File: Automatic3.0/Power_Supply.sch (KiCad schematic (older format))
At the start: 19 parts, among them J1 CONN_01X02, U1 Buck, U2 LM7809

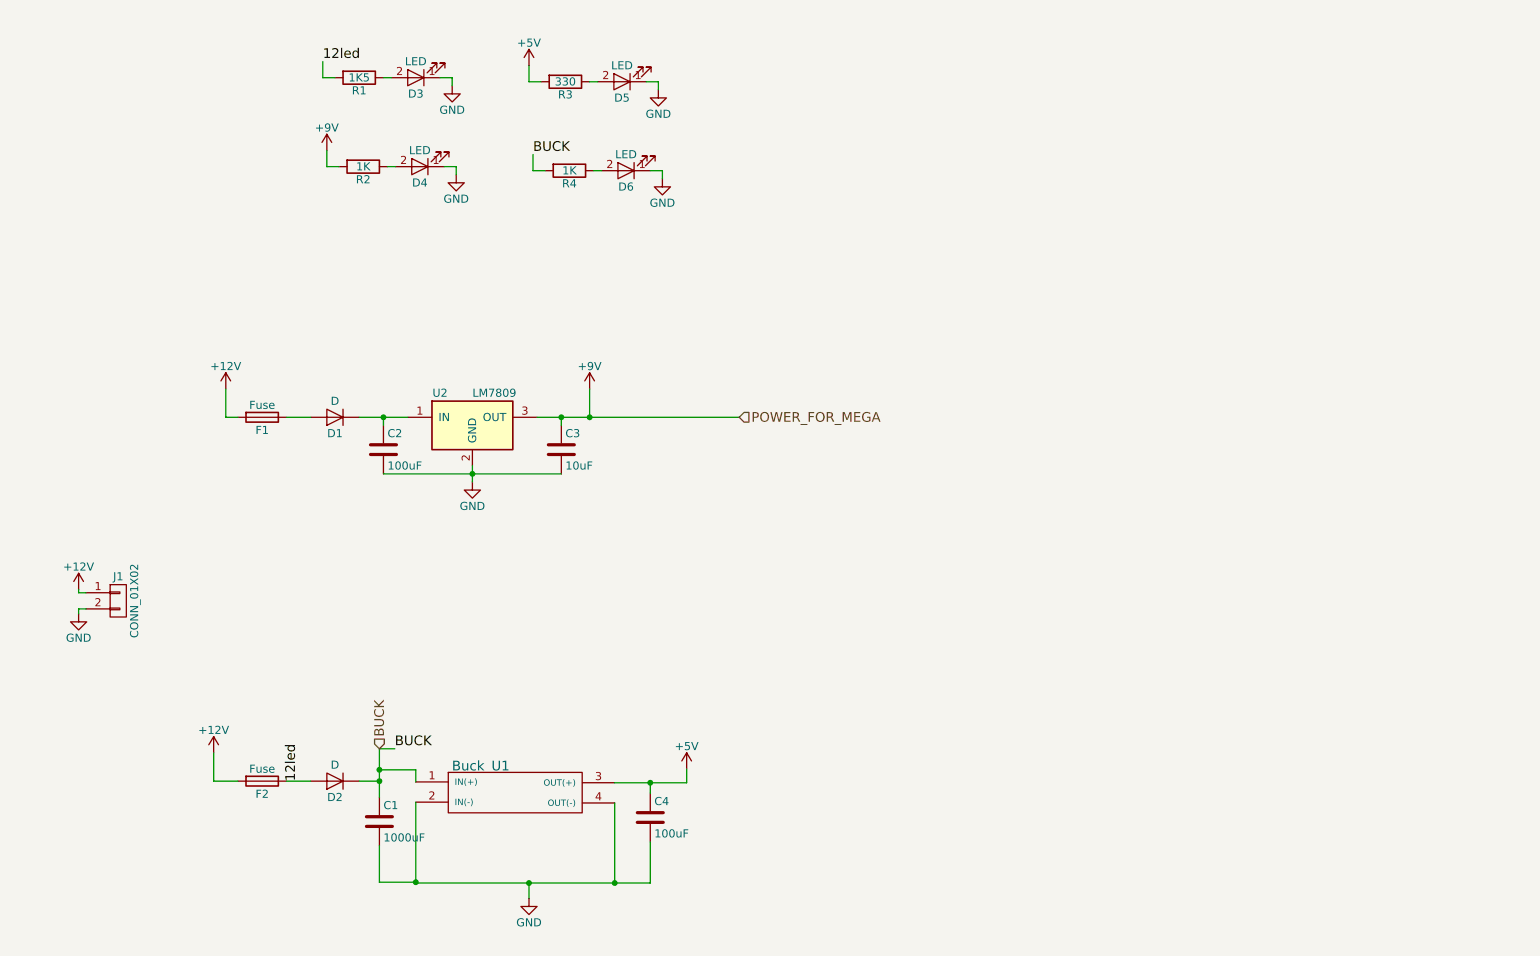
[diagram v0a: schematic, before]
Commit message: Created new schemetic for automatic
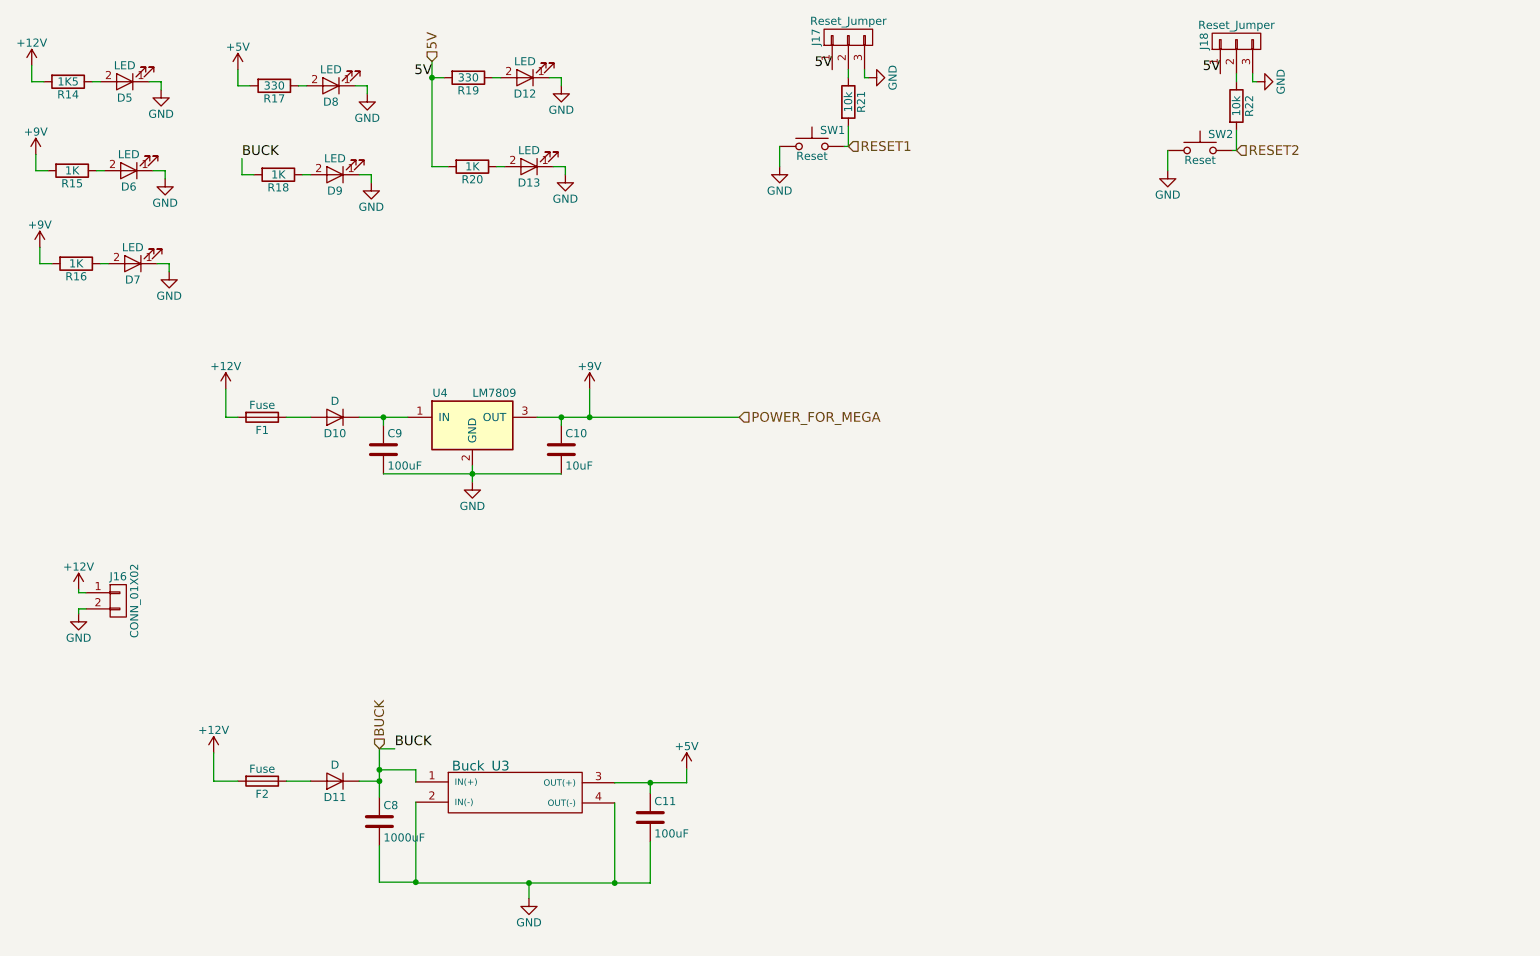
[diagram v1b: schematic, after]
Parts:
- added D12, D13, D7: LED, modFiles:LED_D3.0mm, symbol LED
- added J17, J18: Reset_Jumper, Pin_Headers:Pin_Header_Straight_1x03_Pitch2.54mm, symbol CONN_01X03
- added R16, R20: 1K, modFiles:Resistor_small, symbol R
- added R19: 330, Resistors_THT:R_Axial_DIN0207_L6.3mm_D2.5mm_P10.16mm_Horizontal, symbol R
- added R21, R22: 10k, modFiles:Resistor_small, symbol R
- added SW1, SW2: Reset, modFiles:Push_Button, symbol SW_Push
- renumbered C3 to C10, C4 to C11, C1 to C8, C2 to C9, D1 to D10, D2 to D11, D3 to D5, D4 to D6, D5 to D8, D6 to D9, J1 to J16, R1 to R14, R2 to R15, R3 to R17, R4 to R18, U1 to U3, U2 to U4
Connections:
- net +12V: now also R14.2
- net +9V: now also R16.2
- net GND: now also D12.1 (K), D13.1 (K), D7.1 (K), J17.3 (P3), J18.3 (P3), SW1.1, SW2.1
- net 12led: no longer names the net of D11.2 (A), F2.1
- net 12led: no longer R14.2
- new net: D12.2 (A), R19.1
- new net: D13.2 (A), R20.1
- new net: J17.2 (P2), R21.1
- new net: J18.2 (P2), R22.1
- new net: D7.2 (A), R16.1
- new net 5V: J17.1 (P1), J18.1 (P1), R19.2, R20.2
- new net RESET1: R21.2, SW1.2
- new net RESET2: R22.2, SW2.2
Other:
- moved on the sheet: D5, D6, D8, D9, R14, R15, R17, R18

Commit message: Modified the automatic circuit
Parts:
- D12, D13, D8: value LED -> LED_5V
- D5: value LED -> LED_12V
- D6: value LED -> LED_9V
- D9: value LED -> LED_BUCK
- R17, R19: footprint Resistors_THT:R_Axial_DIN0207_L6.3mm_D2.5mm_P10.16mm_Horizontal -> modFiles:Resistor_small
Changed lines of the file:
@@
 LIBS:zetex
 LIBS:Zilog
-LIBS:Automatic3-cache
+LIBS:Power_Supply-cache
 EELAYER 25 0
 EELAYER END
 $Descr A4 11693 8268
 encoding utf-8
-Sheet 1 2
+Sheet 1 1
 Title ""
 Date ""
@@
 $EndDescr
 $Comp
-L +12V #PWR030
+L +12V #PWR035
 U 1 1 5ADD8405
 P 1400 1225
-F 0 "#PWR030" H 1400 1075 50  0001 C CNN
+F 0 "#PWR035" H 1400 1075 50  0001 C CNN
 F 1 "+12V" H 1400 1365 50  0000 C CNN
 F 2 "" H 1400 1225 50  0001 C CNN
@@
 F 0 "R17" V 2980 1350 50  0000 C CNN
 F 1 "330" V 2900 1350 50  0000 C CNN
-F 2 "Resistors_THT:R_Axial_DIN0207_L6.3mm_D2.5mm_P10.16mm_Horizontal" V 2830 1350 50  0001 C CNN
+F 2 "modFiles:Resistor_small" V 2830 1350 50  0001 C CNN
 F 3 "" H 2900 1350 50  0001 C CNN
 	1    2900 1350
@@
 P 3250 1350
 F 0 "D8" H 3250 1450 50  0000 C CNN
-F 1 "LED" H 3250 1250 50  0000 C CNN
+F 1 "LED_5V" H 3250 1250 50  0000 C CNN
 F 2 "modFiles:LED_D3.0mm" H 3250 1350 50  0001 C CNN
 F 3 "" H 3250 1350 50  0001 C CNN
@@
 $EndComp
 $Comp
-L GND #PWR031
+L GND #PWR036
 U 1 1 5ADD84AA
 P 3475 1400
-F 0 "#PWR031" H 3475 1150 50  0001 C CNN
+F 0 "#PWR036" H 3475 1150 50  0001 C CNN
 F 1 "GND" H 3475 1250 50  0000 C CNN
 F 2 "" H 3475 1400 50  0001 C CNN
@@
 P 3275 1900
 F 0 "D9" H 3275 2000 50  0000 C CNN
-F 1 "LED" H 3275 1800 50  0000 C CNN
+F 1 "LED_BUCK" H 3275 1800 50  0000 C CNN
 F 2 "modFiles:LED_D3.0mm" H 3275 1900 50  0001 C CNN
 F 3 "" H 3275 1900 50  0001 C CNN
@@
 $EndComp
 $Comp
-L GND #PWR032
+L GND #PWR037
 U 1 1 5ADD8645
 P 3500 1950
-F 0 "#PWR032" H 3500 1700 50  0001 C CNN
+F 0 "#PWR037" H 3500 1700 50  0001 C CNN
 F 1 "GND" H 3500 1800 50  0000 C CNN
 F 2 "" H 3500 1950 50  0001 C CNN
@@
 P 1975 1325
 F 0 "D5" H 1975 1425 50  0000 C CNN
-F 1 "LED" H 1975 1225 50  0000 C CNN
+F 1 "LED_12V" H 1975 1225 50  0000 C CNN
 F 2 "modFiles:LED_D3.0mm" H 1975 1325 50  0001 C CNN
 F 3 "" H 1975 1325 50  0001 C CNN
@@
 $EndComp
 $Comp
-L GND #PWR033
+L GND #PWR038
 U 1 1 5ADD88DA
 P 2200 1375
-F 0 "#PWR033" H 2200 1125 50  0001 C CNN
+F 0 "#PWR038" H 2200 1125 50  0001 C CNN
 F 1 "GND" H 2200 1225 50  0000 C CNN
 F 2 "" H 2200 1375 50  0001 C CNN
@@
 P 2000 1875
 F 0 "D6" H 2000 1975 50  0000 C CNN
-F 1 "LED" H 2000 1775 50  0000 C CNN
+F 1 "LED_9V" H 2000 1775 50  0000 C CNN
 F 2 "modFiles:LED_D3.0mm" H 2000 1875 50  0001 C CNN
 F 3 "" H 2000 1875 50  0001 C CNN
@@
 $EndComp
 $Comp
-L GND #PWR034
+L GND #PWR039
 U 1 1 5ADD88F7
 P 2225 1925
-F 0 "#PWR034" H 2225 1675 50  0001 C CNN
+F 0 "#PWR039" H 2225 1675 50  0001 C CNN
 F 1 "GND" H 2225 1775 50  0000 C CNN
 F 2 "" H 2225 1925 50  0001 C CNN
@@
 $EndComp
 $Comp
-L +9V #PWR035
+L +9V #PWR040
 U 1 1 5ADD8969
 P 1425 1775
-F 0 "#PWR035" H 1425 1625 50  0001 C CNN
+F 0 "#PWR040" H 1425 1625 50  0001 C CNN
 F 1 "+9V" H 1425 1915 50  0000 C CNN
 F 2 "" H 1425 1775 50  0001 C CNN
@@
 $EndComp
 $Comp
-L +5V #PWR036
+L +5V #PWR041
 U 1 1 5ADD89A5
 P 2675 1250
-F 0 "#PWR036" H 2675 1100 50  0001 C CNN
+F 0 "#PWR041" H 2675 1100 50  0001 C CNN
 F 1 "+5V" H 2675 1390 50  0000 C CNN
 F 2 "" H 2675 1250 50  0001 C CNN
@@
 $EndComp
 $Comp
-L +12V #PWR037
+L +12V #PWR042
 U 1 1 5ADD8D0E
 P 2600 3225
-F 0 "#PWR037" H 2600 3075 50  0001 C CNN
+F 0 "#PWR042" H 2600 3075 50  0001 C CNN
 F 1 "+12V" H 2600 3365 50  0000 C CNN
 F 2 "" H 2600 3225 50  0001 C CNN
@@
 $EndComp
 $Comp
-L +9V #PWR038
+L +9V #PWR043
 U 1 1 5ADD8DBB
 P 4850 3225
-F 0 "#PWR038" H 4850 3075 50  0001 C CNN
+F 0 "#PWR043" H 4850 3075 50  0001 C CNN
 F 1 "+9V" H 4850 3365 50  0000 C CNN
 F 2 "" H 4850 3225 50  0001 C CNN
@@
 POWER_FOR_MEGA
 $Comp
-L GND #PWR039
+L GND #PWR044
 U 1 1 5ADD935A
 P 4125 3800
-F 0 "#PWR039" H 4125 3550 50  0001 C CNN
+F 0 "#PWR044" H 4125 3550 50  0001 C CNN
 F 1 "GND" H 4125 3650 50  0000 C CNN
 F 2 "" H 4125 3800 50  0001 C CNN
@@
 $EndComp
 $Comp
-L +12V #PWR040
+L +12V #PWR045
 U 1 1 5ADDA23F
 P 2525 5475
-F 0 "#PWR040" H 2525 5325 50  0001 C CNN
+F 0 "#PWR045" H 2525 5325 50  0001 C CNN
 F 1 "+12V" H 2525 5615 50  0000 C CNN
 F 2 "" H 2525 5475 50  0001 C CNN
@@
 $EndComp
 $Comp
-L GND #PWR041
+L GND #PWR046
 U 1 1 5ADDA376
 P 4475 6375
-F 0 "#PWR041" H 4475 6125 50  0001 C CNN
+F 0 "#PWR046" H 4475 6125 50  0001 C CNN
 F 1 "GND" H 4475 6225 50  0000 C CNN
 F 2 "" H 4475 6375 50  0001 C CNN
@@
 $EndComp
 $Comp
-L +5V #PWR042
+L +5V #PWR047
 U 1 1 5ADDA3B0
 P 5450 5575
-F 0 "#PWR042" H 5450 5425 50  0001 C CNN
+F 0 "#PWR047" H 5450 5425 50  0001 C CNN
 F 1 "+5V" H 5450 5715 50  0000 C CNN
 F 2 "" H 5450 5575 50  0001 C CNN
@@
 $EndComp
 $Comp
-L +12V #PWR043
+L +12V #PWR048
 U 1 1 5ADDD1E7
 P 1690 4465
-F 0 "#PWR043" H 1690 4315 50  0001 C CNN
+F 0 "#PWR048" H 1690 4315 50  0001 C CNN
 F 1 "+12V" H 1690 4605 50  0000 C CNN
 F 2 "" H 1690 4465 50  0001 C CNN
@@
 $EndComp
 $Comp
-L GND #PWR044
+L GND #PWR049
 U 1 1 5ADDD3BB
 P 1690 4615
-F 0 "#PWR044" H 1690 4365 50  0001 C CNN
+F 0 "#PWR049" H 1690 4365 50  0001 C CNN
 F 1 "GND" H 1690 4465 50  0000 C CNN
 F 2 "" H 1690 4615 50  0001 C CNN
@@
 F 0 "R19" V 4180 1300 50  0000 C CNN
 F 1 "330" V 4100 1300 50  0000 C CNN
-F 2 "Resistors_THT:R_Axial_DIN0207_L6.3mm_D2.5mm_P10.16mm_Horizontal" V 4030 1300 50  0001 C CNN
+F 2 "modFiles:Resistor_small" V 4030 1300 50  0001 C CNN
 F 3 "" H 4100 1300 50  0001 C CNN
 	1    4100 1300
@@
 P 4450 1300
 F 0 "D12" H 4450 1400 50  0000 C CNN
-F 1 "LED" H 4450 1200 50  0000 C CNN
+F 1 "LED_5V" H 4450 1200 50  0000 C CNN
 F 2 "modFiles:LED_D3.0mm" H 4450 1300 50  0001 C CNN
 F 3 "" H 4450 1300 50  0001 C CNN
@@
 $EndComp
 $Comp
-L GND #PWR045
+L GND #PWR050
 U 1 1 5B1412F8
 P 4675 1350
-F 0 "#PWR045" H 4675 1100 50  0001 C CNN
+F 0 "#PWR050" H 4675 1100 50  0001 C CNN
 F 1 "GND" H 4675 1200 50  0000 C CNN
 F 2 "" H 4675 1350 50  0001 C CNN
@@
 P 4475 1850
 F 0 "D13" H 4475 1950 50  0000 C CNN
-F 1 "LED" H 4475 1750 50  0000 C CNN
+F 1 "LED_5V" H 4475 1750 50  0000 C CNN
 F 2 "modFiles:LED_D3.0mm" H 4475 1850 50  0001 C CNN
 F 3 "" H 4475 1850 50  0001 C CNN
@@
 $EndComp
 $Comp
-L GND #PWR046
+L GND #PWR051
 U 1 1 5B14130A
 P 4700 1900
-F 0 "#PWR046" H 4700 1650 50  0001 C CNN
+F 0 "#PWR051" H 4700 1650 50  0001 C CNN
 F 1 "GND" H 4700 1750 50  0000 C CNN
 F 2 "" H 4700 1900 50  0001 C CNN
@@
 $EndComp
 $Comp
-L GND #PWR047
+L GND #PWR052
 U 1 1 5B1417E4
 P 6025 1850
-F 0 "#PWR047" H 6025 1600 50  0001 C CNN
+F 0 "#PWR052" H 6025 1600 50  0001 C CNN
 F 1 "GND" H 6025 1700 50  0000 C CNN
 F 2 "" H 6025 1850 50  0001 C CNN
@@
 5V
 $Comp
-L GND #PWR048
+L GND #PWR053
 U 1 1 5B14194B
 P 6575 1300
-F 0 "#PWR048" H 6575 1050 50  0001 C CNN
+F 0 "#PWR053" H 6575 1050 50  0001 C CNN
 F 1 "GND" H 6575 1150 50  0000 C CNN
 F 2 "" H 6575 1300 50  0001 C CNN
@@
 $EndComp
 $Comp
-L GND #PWR049
+L GND #PWR054
 U 1 1 5B142045
 P 8425 1875
-F 0 "#PWR049" H 8425 1625 50  0001 C CNN
+F 0 "#PWR054" H 8425 1625 50  0001 C CNN
 F 1 "GND" H 8425 1725 50  0000 C CNN
 F 2 "" H 8425 1875 50  0001 C CNN
@@
 5V
 $Comp
-L GND #PWR050
+L GND #PWR055
 U 1 1 5B14204C
 P 8975 1325
-F 0 "#PWR050" H 8975 1075 50  0001 C CNN
+F 0 "#PWR055" H 8975 1075 50  0001 C CNN
 F 1 "GND" H 8975 1175 50  0000 C CNN
 F 2 "" H 8975 1325 50  0001 C CNN
@@
 $EndComp
 $Comp
-L GND #PWR051
+L GND #PWR056
 U 1 1 5B14315F
 P 2250 2500
-F 0 "#PWR051" H 2250 2250 50  0001 C CNN
+F 0 "#PWR056" H 2250 2250 50  0001 C CNN
 F 1 "GND" H 2250 2350 50  0000 C CNN
 F 2 "" H 2250 2500 50  0001 C CNN
@@
 $EndComp
 $Comp
-L +9V #PWR052
+L +9V #PWR057
 U 1 1 5B143165
 P 1450 2350
-F 0 "#PWR052" H 1450 2200 50  0001 C CNN
+F 0 "#PWR057" H 1450 2200 50  0001 C CNN
 F 1 "+9V" H 1450 2490 50  0000 C CNN
 F 2 "" H 1450 2350 50  0001 C CNN

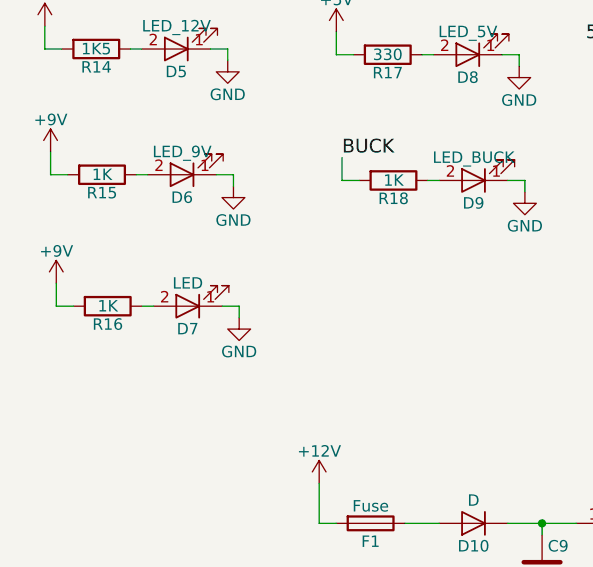
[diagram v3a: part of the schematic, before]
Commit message: added the jst connector
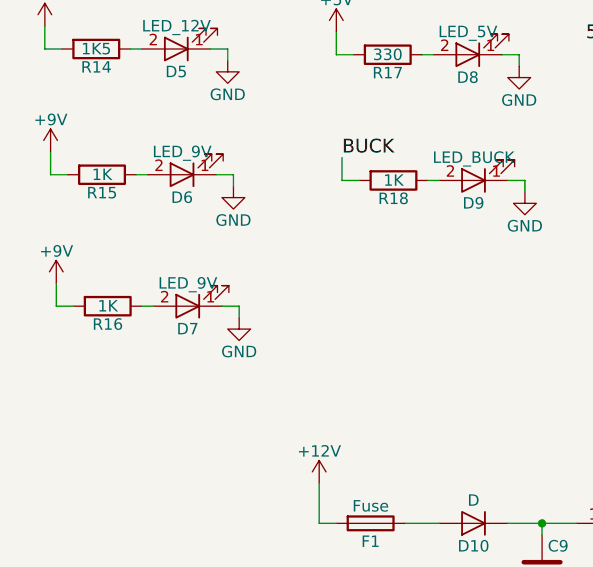
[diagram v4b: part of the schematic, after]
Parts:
- D7: value LED -> LED_9V
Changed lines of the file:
@@
 LIBS:contrib
 LIBS:valves
-LIBS:Prashant_library
 LIBS:74xgxx
 LIBS:ac-dc
@@
 LIBS:ftdi
 LIBS:gennum
-LIBS:graphic
 LIBS:hc11
 LIBS:ir
 LIBS:Lattice
 LIBS:leds
-LIBS:logo
 LIBS:maxim
 LIBS:mechanical
@@
 LIBS:zetex
 LIBS:Zilog
+LIBS:Prashant_library
 LIBS:Automatic3-cache
 EELAYER 25 0
@@
 $Descr A4 11693 8268
 encoding utf-8
-Sheet 1 2
+Sheet 2 2
 Title ""
 Date ""
@@
 $EndDescr
 $Comp
-L +12V #PWR043
+L +12V #PWR044
 U 1 1 5ADD8405
 P 1400 1225
-F 0 "#PWR043" H 1400 1075 50  0001 C CNN
+F 0 "#PWR044" H 1400 1075 50  0001 C CNN
 F 1 "+12V" H 1400 1365 50  0000 C CNN
 F 2 "" H 1400 1225 50  0001 C CNN
@@
 $EndComp
 $Comp
-L GND #PWR044
+L GND #PWR045
 U 1 1 5ADD84AA
 P 3475 1400
-F 0 "#PWR044" H 3475 1150 50  0001 C CNN
+F 0 "#PWR045" H 3475 1150 50  0001 C CNN
 F 1 "GND" H 3475 1250 50  0000 C CNN
 F 2 "" H 3475 1400 50  0001 C CNN
@@
 $EndComp
 $Comp
-L GND #PWR045
+L GND #PWR046
 U 1 1 5ADD8645
 P 3500 1950
-F 0 "#PWR045" H 3500 1700 50  0001 C CNN
+F 0 "#PWR046" H 3500 1700 50  0001 C CNN
 F 1 "GND" H 3500 1800 50  0000 C CNN
 F 2 "" H 3500 1950 50  0001 C CNN
@@
 $EndComp
 $Comp
-L GND #PWR046
+L GND #PWR047
 U 1 1 5ADD88DA
 P 2200 1375
-F 0 "#PWR046" H 2200 1125 50  0001 C CNN
+F 0 "#PWR047" H 2200 1125 50  0001 C CNN
 F 1 "GND" H 2200 1225 50  0000 C CNN
 F 2 "" H 2200 1375 50  0001 C CNN
@@
 $EndComp
 $Comp
-L GND #PWR047
+L GND #PWR048
 U 1 1 5ADD88F7
 P 2225 1925
-F 0 "#PWR047" H 2225 1675 50  0001 C CNN
+F 0 "#PWR048" H 2225 1675 50  0001 C CNN
 F 1 "GND" H 2225 1775 50  0000 C CNN
 F 2 "" H 2225 1925 50  0001 C CNN
@@
 $EndComp
 $Comp
-L +9V #PWR048
+L +9V #PWR049
 U 1 1 5ADD8969
 P 1425 1775
-F 0 "#PWR048" H 1425 1625 50  0001 C CNN
+F 0 "#PWR049" H 1425 1625 50  0001 C CNN
 F 1 "+9V" H 1425 1915 50  0000 C CNN
 F 2 "" H 1425 1775 50  0001 C CNN
@@
 $EndComp
 $Comp
-L +5V #PWR049
+L +5V #PWR050
 U 1 1 5ADD89A5
 P 2675 1250
-F 0 "#PWR049" H 2675 1100 50  0001 C CNN
+F 0 "#PWR050" H 2675 1100 50  0001 C CNN
 F 1 "+5V" H 2675 1390 50  0000 C CNN
 F 2 "" H 2675 1250 50  0001 C CNN
@@
 $EndComp
 $Comp
-L +12V #PWR050
+L +12V #PWR051
 U 1 1 5ADD8D0E
 P 2600 3225
-F 0 "#PWR050" H 2600 3075 50  0001 C CNN
+F 0 "#PWR051" H 2600 3075 50  0001 C CNN
 F 1 "+12V" H 2600 3365 50  0000 C CNN
 F 2 "" H 2600 3225 50  0001 C CNN
@@
 $EndComp
 $Comp
-L +9V #PWR051
+L +9V #PWR052
 U 1 1 5ADD8DBB
 P 4850 3225
-F 0 "#PWR051" H 4850 3075 50  0001 C CNN
+F 0 "#PWR052" H 4850 3075 50  0001 C CNN
 F 1 "+9V" H 4850 3365 50  0000 C CNN
 F 2 "" H 4850 3225 50  0001 C CNN
@@
 POWER_FOR_MEGA
 $Comp
-L GND #PWR052
+L GND #PWR053
 U 1 1 5ADD935A
 P 4125 3800
-F 0 "#PWR052" H 4125 3550 50  0001 C CNN
+F 0 "#PWR053" H 4125 3550 50  0001 C CNN
 F 1 "GND" H 4125 3650 50  0000 C CNN
 F 2 "" H 4125 3800 50  0001 C CNN
@@
 $EndComp
 $Comp
-L +12V #PWR053
+L +12V #PWR054
 U 1 1 5ADDA23F
 P 2525 5475
-F 0 "#PWR053" H 2525 5325 50  0001 C CNN
+F 0 "#PWR054" H 2525 5325 50  0001 C CNN
 F 1 "+12V" H 2525 5615 50  0000 C CNN
 F 2 "" H 2525 5475 50  0001 C CNN
@@
 $EndComp
 $Comp
-L GND #PWR054
+L GND #PWR055
 U 1 1 5ADDA376
 P 4475 6375
-F 0 "#PWR054" H 4475 6125 50  0001 C CNN
+F 0 "#PWR055" H 4475 6125 50  0001 C CNN
 F 1 "GND" H 4475 6225 50  0000 C CNN
 F 2 "" H 4475 6375 50  0001 C CNN
@@
 $EndComp
 $Comp
-L +5V #PWR055
+L +5V #PWR056
 U 1 1 5ADDA3B0
 P 5450 5575
-F 0 "#PWR055" H 5450 5425 50  0001 C CNN
+F 0 "#PWR056" H 5450 5425 50  0001 C CNN
 F 1 "+5V" H 5450 5715 50  0000 C CNN
 F 2 "" H 5450 5575 50  0001 C CNN
@@
 $EndComp
 $Comp
-L +12V #PWR056
+L +12V #PWR057
 U 1 1 5ADDD1E7
 P 1690 4465
-F 0 "#PWR056" H 1690 4315 50  0001 C CNN
+F 0 "#PWR057" H 1690 4315 50  0001 C CNN
 F 1 "+12V" H 1690 4605 50  0000 C CNN
 F 2 "" H 1690 4465 50  0001 C CNN
@@
 $EndComp
 $Comp
-L GND #PWR057
+L GND #PWR058
 U 1 1 5ADDD3BB
 P 1690 4615
-F 0 "#PWR057" H 1690 4365 50  0001 C CNN
+F 0 "#PWR058" H 1690 4365 50  0001 C CNN
 F 1 "GND" H 1690 4465 50  0000 C CNN
 F 2 "" H 1690 4615 50  0001 C CNN
@@
 $EndComp
 $Comp
-L GND #PWR058
+L GND #PWR059
 U 1 1 5B1412F8
 P 4675 1350
-F 0 "#PWR058" H 4675 1100 50  0001 C CNN
+F 0 "#PWR059" H 4675 1100 50  0001 C CNN
 F 1 "GND" H 4675 1200 50  0000 C CNN
 F 2 "" H 4675 1350 50  0001 C CNN
@@
 $EndComp
 $Comp
-L GND #PWR059
+L GND #PWR060
 U 1 1 5B14130A
 P 4700 1900
-F 0 "#PWR059" H 4700 1650 50  0001 C CNN
+F 0 "#PWR060" H 4700 1650 50  0001 C CNN
 F 1 "GND" H 4700 1750 50  0000 C CNN
 F 2 "" H 4700 1900 50  0001 C CNN
@@
 $EndComp
 $Comp
-L GND #PWR060
+L GND #PWR061
 U 1 1 5B1417E4
 P 6025 1850
-F 0 "#PWR060" H 6025 1600 50  0001 C CNN
+F 0 "#PWR061" H 6025 1600 50  0001 C CNN
 F 1 "GND" H 6025 1700 50  0000 C CNN
 F 2 "" H 6025 1850 50  0001 C CNN
@@
 5V
 $Comp
-L GND #PWR061
+L GND #PWR062
 U 1 1 5B14194B
 P 6575 1300
-F 0 "#PWR061" H 6575 1050 50  0001 C CNN
+F 0 "#PWR062" H 6575 1050 50  0001 C CNN
 F 1 "GND" H 6575 1150 50  0000 C CNN
 F 2 "" H 6575 1300 50  0001 C CNN
@@
 $EndComp
 $Comp
-L GND #PWR062
+L GND #PWR063
 U 1 1 5B142045
 P 8425 1875
-F 0 "#PWR062" H 8425 1625 50  0001 C CNN
+F 0 "#PWR063" H 8425 1625 50  0001 C CNN
 F 1 "GND" H 8425 1725 50  0000 C CNN
 F 2 "" H 8425 1875 50  0001 C CNN
@@
 5V
 $Comp
-L GND #PWR063
+L GND #PWR064
 U 1 1 5B14204C
 P 8975 1325
-F 0 "#PWR063" H 8975 1075 50  0001 C CNN
+F 0 "#PWR064" H 8975 1075 50  0001 C CNN
 F 1 "GND" H 8975 1175 50  0000 C CNN
 F 2 "" H 8975 1325 50  0001 C CNN
@@
 P 2025 2450
 F 0 "D7" H 2025 2550 50  0000 C CNN
-F 1 "LED" H 2025 2350 50  0000 C CNN
+F 1 "LED_9V" H 2025 2350 50  0000 C CNN
 F 2 "modFiles:LED_D3.0mm" H 2025 2450 50  0001 C CNN
 F 3 "" H 2025 2450 50  0001 C CNN
@@
 $EndComp
 $Comp
-L GND #PWR064
+L GND #PWR065
 U 1 1 5B14315F
 P 2250 2500
-F 0 "#PWR064" H 2250 2250 50  0001 C CNN
+F 0 "#PWR065" H 2250 2250 50  0001 C CNN
 F 1 "GND" H 2250 2350 50  0000 C CNN
 F 2 "" H 2250 2500 50  0001 C CNN
@@
 $EndComp
 $Comp
-L +9V #PWR065
+L +9V #PWR066
 U 1 1 5B143165
 P 1450 2350
-F 0 "#PWR065" H 1450 2200 50  0001 C CNN
+F 0 "#PWR066" H 1450 2200 50  0001 C CNN
 F 1 "+9V" H 1450 2490 50  0000 C CNN
 F 2 "" H 1450 2350 50  0001 C CNN
